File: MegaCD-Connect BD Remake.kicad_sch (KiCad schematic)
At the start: 17 parts, among them IC1 GAL22V10, IC2 74HC374, IC3 74HC374, IC4 74LS10, IC5 74HC245, IC6 74HC245, J1 MD EXPANSION, J2 CD EXPANSION, J3 TREE HOUSE

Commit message: Update PCB to Version 2.1 * Moved /TRDIR from pin 23 to pin 15 * Added GAL20V8 Logic * Updated Labels for Tree House Connection, TH1 and TH2 * Added an iBom * Updated the ReadMe
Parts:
- IC4: value 74LS10 -> 74ACT10
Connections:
- net GND: no longer IC1.15 (IO9)
- net TR_DIR: now also IC1.15 (IO9); no longer IC1.23 (IO1)
- no-connect marks 11 -> 12
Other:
- moved on the sheet: IC4B
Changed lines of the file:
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@@
   (title_block
     (title "MegaCD Connect BD Remake")
-    (date "2023-05-14")
-    (rev "V2.0")
+    (date "2023-06-03")
+    (rev "V2.1")
     (company "Board Folk")
   )
@@
   (junction (at 76.2 82.55) (diameter 0) (color 0 0 0 0)
   )
-  (junction (at 240.03 133.35) (diameter 0) (color 0 0 0 0)
-  )
   (junction (at 36.83 184.15) (diameter 0) (color 0 0 0 0)
   )
-  (junction (at 248.92 125.73) (diameter 0) (color 0 0 0 0)
+  (junction (at 252.73 125.73) (diameter 0) (color 0 0 0 0)
   )
   (junction (at 152.4 76.2) (diameter 0) (color 0 0 0 0)
@@
   (no_connect (at 240.03 128.27))
   (no_connect (at 240.03 123.19))
+  (no_connect (at 240.03 110.49))
   (no_connect (at 38.1 118.11))
   (no_connect (at 240.03 125.73))
@@
     (stroke (width 0) (type default))
   )
-  (wire (pts (xy 266.7 123.19) (xy 267.97 123.19))
+  (wire (pts (xy 270.51 123.19) (xy 271.78 123.19))
     (stroke (width 0) (type default))
   )
@@
     (stroke (width 0) (type default))
   )
-  (wire (pts (xy 240.03 130.81) (xy 240.03 133.35))
-    (stroke (width 0) (type default))
-  )
   (bus (pts (xy 88.9 149.86) (xy 88.9 152.4))
     (stroke (width 0) (type default))
@@
     (stroke (width 0) (type default))
   )
-  (wire (pts (xy 251.46 123.19) (xy 248.92 123.19))
+  (wire (pts (xy 255.27 123.19) (xy 252.73 123.19))
     (stroke (width 0) (type default))
   )
@@
     (stroke (width 0) (type default))
   )
-  (wire (pts (xy 240.03 110.49) (xy 241.3 110.49))
+  (wire (pts (xy 240.03 130.81) (xy 241.3 130.81))
     (stroke (width 0) (type default))
   )
@@
     (stroke (width 0) (type default))
   )
-  (wire (pts (xy 240.03 120.65) (xy 251.46 120.65))
+  (wire (pts (xy 240.03 120.65) (xy 255.27 120.65))
     (stroke (width 0) (type default))
   )
@@
     (stroke (width 0) (type default))
   )
-  (wire (pts (xy 248.92 123.19) (xy 248.92 125.73))
+  (wire (pts (xy 252.73 123.19) (xy 252.73 125.73))
     (stroke (width 0) (type default))
   )
@@
     (stroke (width 0) (type default))
   )
-  (wire (pts (xy 248.92 125.73) (xy 251.46 125.73))
+  (wire (pts (xy 252.73 125.73) (xy 255.27 125.73))
     (stroke (width 0) (type default))
   )
@@
     (stroke (width 0) (type default))
   )
-  (wire (pts (xy 248.92 125.73) (xy 248.92 129.54))
+  (wire (pts (xy 252.73 125.73) (xy 252.73 129.54))
     (stroke (width 0) (type default))
   )
@@
     )
   )
-  (global_label "~{CDCAS0}" (shape output) (at 267.97 123.19 0) (fields_autoplaced)
+  (global_label "~{CDCAS0}" (shape output) (at 271.78 123.19 0) (fields_autoplaced)
     (effects (font (size 1.27 1.27)) (justify left))
-    (property "Intersheetrefs" "${INTERSHEET_REFS}" (at 278.1934 123.19 0)
+    (property "Intersheetrefs" "${INTERSHEET_REFS}" (at 282.0034 123.19 0)
       (effects (font (size 1.27 1.27)) (justify left) hide)
     )
@@
     )
   )
-  (global_label "TR_DIR" (shape output) (at 241.3 110.49 0) (fields_autoplaced)
+  (global_label "TR_DIR" (shape output) (at 241.3 130.81 0) (fields_autoplaced)
     (effects (font (size 1.27 1.27)) (justify left))
-    (property "Intersheetrefs" "${INTERSHEET_REFS}" (at 250.5558 110.49 0)
+    (property "Intersheetrefs" "${INTERSHEET_REFS}" (at 250.5558 130.81 0)
       (effects (font (size 1.27 1.27)) (justify left) hide)
     )
@@
       (effects (font (size 1.27 1.27)) hide)
     )
-    (property "Datasheet" "~" (at 158.75 177.8 0)
+    (property "Datasheet" "" (at 158.75 177.8 0)
       (effects (font (size 1.27 1.27)) hide)
     )
@@
       (effects (font (size 1.27 1.27)) hide)
     )
-    (property "Datasheet" "~" (at 158.75 185.42 0)
+    (property "Datasheet" "" (at 158.75 185.42 0)
       (effects (font (size 1.27 1.27)) hide)
     )
@@
       (effects (font (size 1.27 1.27)))
     )
-    (property "Value" "74LS10" (at 227.33 152.4 90)
+    (property "Value" "74ACT10" (at 227.33 152.4 90)
       (effects (font (size 1.27 1.27)))
     )
@@
       (effects (font (size 1.27 1.27)) hide)
     )
-    (property "Datasheet" "http://www.ti.com/lit/gpn/sn74LS10" (at 227.33 158.75 0)
+    (property "Datasheet" "" (at 227.33 158.75 0)
       (effects (font (size 1.27 1.27)) hide)
     )
@@
       (effects (font (size 1.27 1.27)) hide)
     )
-    (property "Datasheet" "http://www.ti.com/lit/gpn/sn74HC245" (at 50.8 41.91 0)
+    (property "Datasheet" "" (at 50.8 41.91 0)
       (effects (font (size 1.27 1.27)) hide)
     )
@@
       (effects (font (size 1.27 1.27)) hide)
     )
-    (property "Datasheet" "https://www.ti.com/lit/ds/symlink/cd74hct374.pdf" (at 241.3 41.91 0)
+    (property "Datasheet" "" (at 241.3 41.91 0)
       (effects (font (size 1.27 1.27)) hide)
     )
@@
       (effects (font (size 1.27 1.27)) hide)
     )
-    (property "Datasheet" "~" (at 43.18 151.13 0)
+    (property "Datasheet" "" (at 43.18 151.13 0)
       (effects (font (size 1.27 1.27)) hide)
     )
@@
       (effects (font (size 1.27 1.27)) hide)
     )
-    (property "Datasheet" "~" (at 158.75 170.18 0)
+    (property "Datasheet" "" (at 158.75 170.18 0)
       (effects (font (size 1.27 1.27)) hide)
     )
@@
       (effects (font (size 1.27 1.27)) hide)
     )
-    (property "Datasheet" "http://www.ti.com/lit/gpn/sn74HC245" (at 177.8 41.91 0)
+    (property "Datasheet" "" (at 177.8 41.91 0)
       (effects (font (size 1.27 1.27)) hide)
     )
@@
       (effects (font (size 1.27 1.27)))
     )
-    (property "Value" "74LS10" (at 198.1117 105.41 0)
+    (property "Value" "74ACT10" (at 198.1117 105.41 0)
       (effects (font (size 1.27 1.27)))
     )
@@
       (effects (font (size 1.27 1.27)) hide)
     )
-    (property "Datasheet" "http://www.ti.com/lit/gpn/sn74LS10" (at 198.12 110.49 0)
+    (property "Datasheet" "" (at 198.12 110.49 0)
       (effects (font (size 1.27 1.27)) hide)
     )
@@
       (effects (font (size 1.27 1.27)) hide)
     )
-    (property "Datasheet" "~" (at 158.75 173.99 0)
+    (property "Datasheet" "" (at 158.75 173.99 0)
       (effects (font (size 1.27 1.27)) hide)
     )
@@
     )
   )
-  (symbol (lib_id "74xx:74LS10") (at 259.08 123.19 0) (unit 2)
+  (symbol (lib_id "74xx:74LS10") (at 262.89 123.19 0) (unit 2)
     (in_bom yes) (on_board yes) (dnp no) (fields_autoplaced)
-    (property "Reference" "IC4" (at 259.0717 115.57 0)
+    (property "Reference" "IC4" (at 262.8817 115.57 0)
       (effects (font (size 1.27 1.27)))
     )
-    (property "Value" "74LS10" (at 259.0717 118.11 0)
+    (property "Value" "74ACT10" (at 262.8817 118.11 0)
       (effects (font (size 1.27 1.27)))
     )
-    (property "Footprint" "Package_DIP:DIP-14_W7.62mm_Socket_LongPads" (at 259.08 123.19 0)
+    (property "Footprint" "Package_DIP:DIP-14_W7.62mm_Socket_LongPads" (at 262.89 123.19 0)
       (effects (font (size 1.27 1.27)) hide)
     )
-    (property "Datasheet" "http://www.ti.com/lit/gpn/sn74LS10" (at 259.08 123.19 0)
+    (property "Datasheet" "" (at 262.89 123.19 0)
       (effects (font (size 1.27 1.27)) hide)
     )
@@
       (effects (font (size 1.27 1.27)) hide)
     )
-    (property "Datasheet" "https://www.ti.com/lit/ds/symlink/cd74hct374.pdf" (at 114.3 41.91 0)
+    (property "Datasheet" "" (at 114.3 41.91 0)
       (effects (font (size 1.27 1.27)) hide)
     )
@@
       (effects (font (size 1.27 1.27)) hide)
     )
-    (property "Datasheet" "~" (at 106.68 152.4 0)
+    (property "Datasheet" "" (at 106.68 152.4 0)
       (effects (font (size 1.27 1.27)) hide)
     )
@@
       (effects (font (size 1.27 1.27)) hide)
     )
-    (property "Datasheet" "~" (at 158.75 181.61 0)
+    (property "Datasheet" "" (at 158.75 181.61 0)
       (effects (font (size 1.27 1.27)) hide)
     )
@@
       (effects (font (size 1.27 1.27)))
     )
-    (property "Value" "74LS10" (at 198.1117 120.65 0)
+    (property "Value" "74ACT10" (at 198.1117 120.65 0)
       (effects (font (size 1.27 1.27)))
     )
@@
       (effects (font (size 1.27 1.27)) hide)
     )
-    (property "Datasheet" "http://www.ti.com/lit/gpn/sn74LS10" (at 198.12 125.73 0)
+    (property "Datasheet" "" (at 198.12 125.73 0)
       (effects (font (size 1.27 1.27)) hide)
     )
@@
       (effects (font (size 1.27 1.27)) hide)
     )
-    (property "Datasheet" "http://www.vishay.com/docs/31509/csc.pdf" (at 162.56 143.51 0)
+    (property "Datasheet" "" (at 162.56 143.51 0)
       (effects (font (size 1.27 1.27)) hide)
     )
@@
       (effects (font (size 1.27 1.27)) hide)
     )
-    (property "Datasheet" "~" (at 158.75 166.37 0)
+    (property "Datasheet" "" (at 158.75 166.37 0)
       (effects (font (size 1.27 1.27)) hide)
     )
@@
       (effects (font (size 1.27 1.27)) hide)
     )
-    (property "Datasheet" "~" (at 50.8 93.98 0)
+    (property "Datasheet" "" (at 50.8 93.98 0)
       (effects (font (size 1.27 1.27)) hide)
     )
@@
       (effects (font (size 1.27 1.27)) hide)
     )
-    (property "Datasheet" "http://www.vishay.com/docs/31509/csc.pdf" (at 162.56 105.41 0)
+    (property "Datasheet" "" (at 162.56 105.41 0)
       (effects (font (size 1.27 1.27)) hide)
     )
@@
     )
   )
-  (symbol (lib_id "power:VCC") (at 248.92 129.54 180) (unit 1)
+  (symbol (lib_id "power:VCC") (at 252.73 129.54 180) (unit 1)
     (in_bom yes) (on_board yes) (dnp no)
-    (property "Reference" "#PWR011" (at 248.92 125.73 0)
+    (property "Reference" "#PWR011" (at 252.73 125.73 0)
       (effects (font (size 1.27 1.27)) hide)
     )
-    (property "Value" "VCC" (at 248.92 133.35 0)
+    (property "Value" "VCC" (at 252.73 133.35 0)
       (effects (font (size 1.27 1.27)))
     )
-    (property "Footprint" "" (at 248.92 129.54 0)
+    (property "Footprint" "" (at 252.73 129.54 0)
       (effects (font (size 1.27 1.27)) hide)
     )
-    (property "Datasheet" "" (at 248.92 129.54 0)
+    (property "Datasheet" "" (at 252.73 129.54 0)
       (effects (font (size 1.27 1.27)) hide)
     )

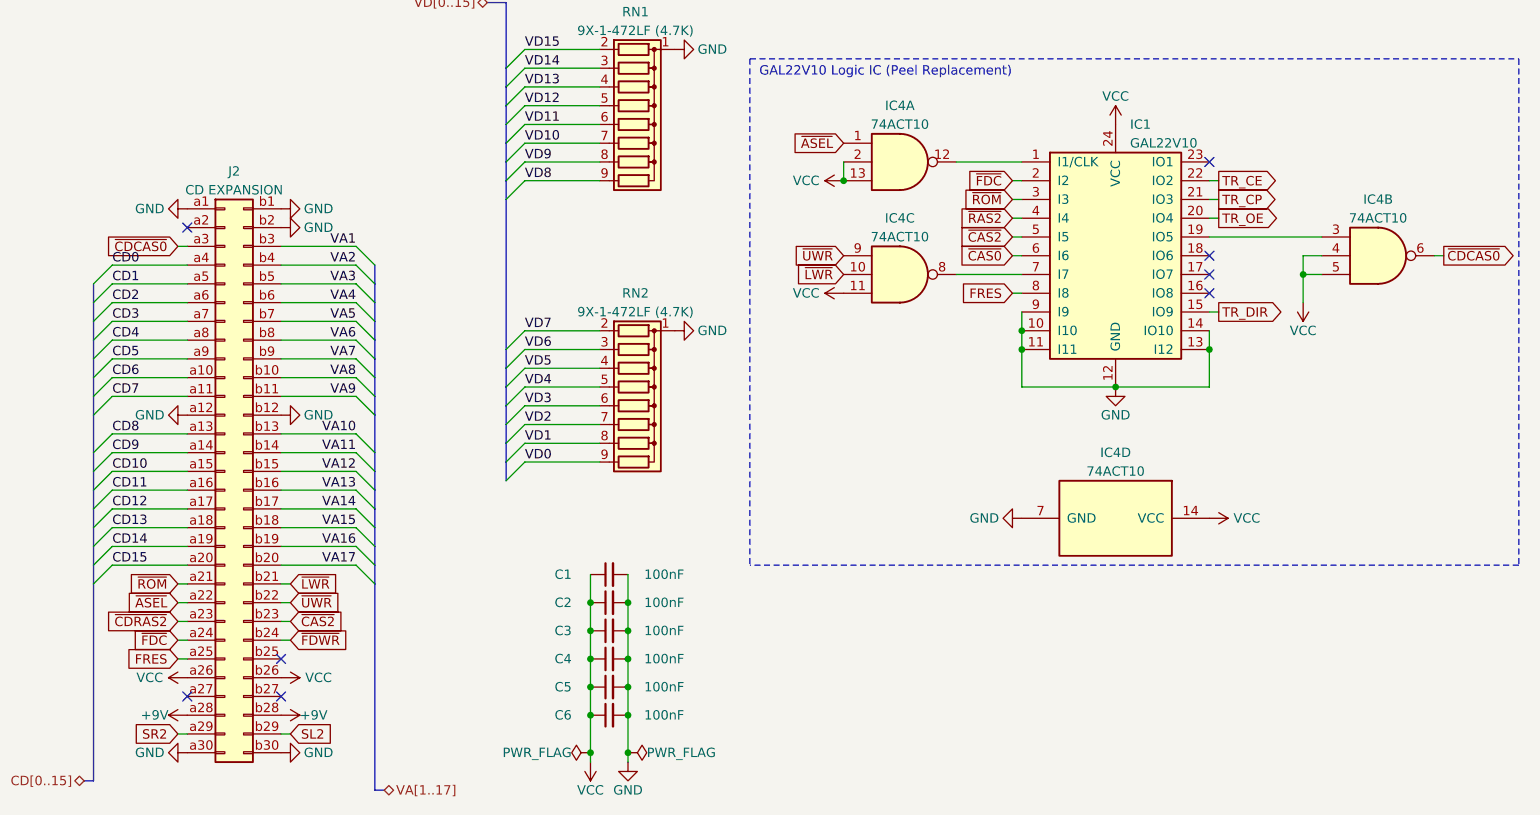
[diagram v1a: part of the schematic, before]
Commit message: Updated PCB to v2.3 removed A26 B26 Linking to VCC and back to 9V instead on the CD Side Only.
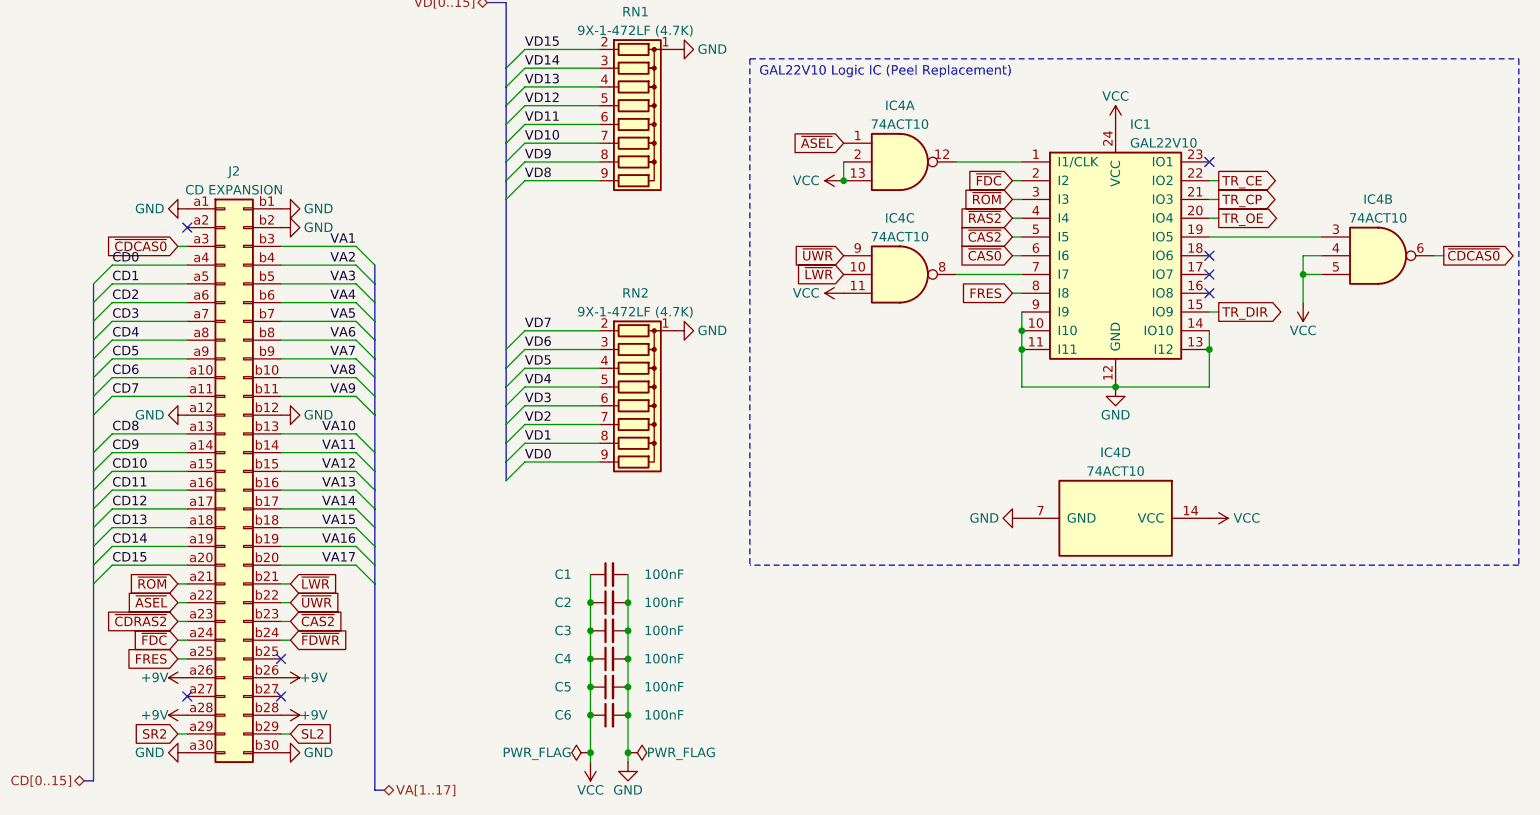
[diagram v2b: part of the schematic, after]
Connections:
- net +9V: now also J2.a26 (Pin_a26), J2.b26 (Pin_b26)
- net VCC: no longer J2.a26 (Pin_a26), J2.b26 (Pin_b26)
